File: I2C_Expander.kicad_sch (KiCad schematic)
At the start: 8 parts, among them U501 PCA9554APW

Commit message: Update pcb database to version 6
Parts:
- C501: symbol Custom:C_US_0805_0.1UF_X7R_10%_50V_HS -> custom:C_US_0805_0.1UF_X7R_10%_50V_HS
- R501, R502: symbol Custom:R_US_0805_1%_HS -> custom:R_US_0805_1%_HS; PartNumber 800235-103 -> 800235-XXX
- R503, R504, R505, R506: symbol Custom:R_US_0805_1%_HS -> custom:R_US_0805_1%_HS; PartNumber 800235-102 -> 800235-XXX
- U501: symbol Custom:PCA9554APW -> custom:PCA9554APW
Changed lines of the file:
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@@
     (effects (font (size 1.27 1.27)) (justify left))
   )
-  (symbol (lib_id "Custom:PCA9554APW") (at 163.83 66.04 0)
+  (symbol (lib_id "custom:PCA9554APW") (at 163.83 66.04 0) (unit 1)
     (in_bom yes) (on_board yes)
     (property "Reference" "U501" (id 0) (at 163.83 36.449 0))
@@
     (pin "9")
   )
-  (symbol (lib_id "Custom:GND_US") (at 179.07 91.44 0)
+  (symbol (lib_id "custom:GND_US") (at 179.07 91.44 0) (unit 1)
     (in_bom yes) (on_board yes)
     (property "Reference" "#PWR0503" (id 0) (at 178.562 94.742 0)
@@
     (pin "1")
   )
-  (symbol (lib_id "Custom:C_US_0805_0.1UF_X7R_10%_50V_HS") (at 190.5 39.37 90)
+  (symbol (lib_id "custom:C_US_0805_0.1UF_X7R_10%_50V_HS") (at 190.5 39.37 90) (unit 1)
     (in_bom yes) (on_board yes)
     (property "Reference" "C501" (id 0) (at 190.5 32.5882 90))
@@
     (pin "2")
   )
-  (symbol (lib_id "Custom:P3V3") (at 179.07 26.67 0)
+  (symbol (lib_id "custom:P3V3") (at 179.07 26.67 0) (unit 1)
     (in_bom yes) (on_board yes)
     (property "Reference" "#PWR0501" (id 0) (at 181.61 25.4 0)
@@
     (pin "1")
   )
-  (symbol (lib_id "Custom:GND_US") (at 198.12 41.91 0)
+  (symbol (lib_id "custom:GND_US") (at 198.12 41.91 0) (unit 1)
     (in_bom yes) (on_board yes)
     (property "Reference" "#PWR0502" (id 0) (at 197.612 45.212 0)
@@
     (pin "1")
   )
-  (symbol (lib_id "Custom:R_US_0805_1%_HS") (at 200.66 97.79 0)
+  (symbol (lib_id "custom:R_US_0805_1%_HS") (at 200.66 97.79 0) (unit 1)
     (in_bom yes) (on_board yes)
     (property "Reference" "R503" (id 0) (at 202.184 96.6216 0)
@@
       (effects (font (size 1.524 1.524)))
     )
-    (property "PartNumber" "800235-102" (id 4) (at 205.232 95.25 90)
-      (effects (font (size 1.524 1.524)) hide)
-    )
-    (pin "1")
-    (pin "2")
-  )
-  (symbol (lib_id "Custom:R_US_0805_1%_HS") (at 207.01 97.79 0)
+    (property "PartNumber" "800235-XXX" (id 4) (at 205.232 95.25 90)
+      (effects (font (size 1.524 1.524)) hide)
+    )
+    (pin "1")
+    (pin "2")
+  )
+  (symbol (lib_id "custom:R_US_0805_1%_HS") (at 207.01 97.79 0) (unit 1)
     (in_bom yes) (on_board yes)
     (property "Reference" "R504" (id 0) (at 208.534 96.6216 0)
@@
       (effects (font (size 1.524 1.524)))
     )
-    (property "PartNumber" "800235-102" (id 4) (at 211.582 95.25 90)
-      (effects (font (size 1.524 1.524)) hide)
-    )
-    (pin "1")
-    (pin "2")
-  )
-  (symbol (lib_id "Custom:R_US_0805_1%_HS") (at 213.36 97.79 0)
+    (property "PartNumber" "800235-XXX" (id 4) (at 211.582 95.25 90)
+      (effects (font (size 1.524 1.524)) hide)
+    )
+    (pin "1")
+    (pin "2")
+  )
+  (symbol (lib_id "custom:R_US_0805_1%_HS") (at 213.36 97.79 0) (unit 1)
     (in_bom yes) (on_board yes)
     (property "Reference" "R505" (id 0) (at 214.884 96.6216 0)
@@
       (effects (font (size 1.524 1.524)))
     )
-    (property "PartNumber" "800235-102" (id 4) (at 217.932 95.25 90)
-      (effects (font (size 1.524 1.524)) hide)
-    )
-    (pin "1")
-    (pin "2")
-  )
-  (symbol (lib_id "Custom:R_US_0805_1%_HS") (at 226.06 97.79 0)
+    (property "PartNumber" "800235-XXX" (id 4) (at 217.932 95.25 90)
+      (effects (font (size 1.524 1.524)) hide)
+    )
+    (pin "1")
+    (pin "2")
+  )
+  (symbol (lib_id "custom:R_US_0805_1%_HS") (at 226.06 97.79 0) (unit 1)
     (in_bom yes) (on_board yes)
     (property "Reference" "R506" (id 0) (at 227.584 96.6216 0)
@@
       (effects (font (size 1.524 1.524)))
     )
-    (property "PartNumber" "800235-102" (id 4) (at 230.632 95.25 90)
-      (effects (font (size 1.524 1.524)) hide)
-    )
-    (pin "1")
-    (pin "2")
-  )
-  (symbol (lib_id "Custom:GND_US") (at 200.66 105.41 0)
+    (property "PartNumber" "800235-XXX" (id 4) (at 230.632 95.25 90)
+      (effects (font (size 1.524 1.524)) hide)
+    )
+    (pin "1")
+    (pin "2")
+  )
+  (symbol (lib_id "custom:GND_US") (at 200.66 105.41 0) (unit 1)
     (in_bom yes) (on_board yes)
     (property "Reference" "#PWR0505" (id 0) (at 200.152 108.712 0)
@@
     (pin "1")
   )
-  (symbol (lib_id "Custom:GND_US") (at 207.01 105.41 0)
+  (symbol (lib_id "custom:GND_US") (at 207.01 105.41 0) (unit 1)
     (in_bom yes) (on_board yes)
     (property "Reference" "#PWR0506" (id 0) (at 206.502 108.712 0)
@@
     (pin "1")
   )
-  (symbol (lib_id "Custom:GND_US") (at 213.36 105.41 0)
+  (symbol (lib_id "custom:GND_US") (at 213.36 105.41 0) (unit 1)
     (in_bom yes) (on_board yes)
     (property "Reference" "#PWR0507" (id 0) (at 212.852 108.712 0)
@@
     (pin "1")
   )
-  (symbol (lib_id "Custom:GND_US") (at 226.06 105.41 0)
+  (symbol (lib_id "custom:GND_US") (at 226.06 105.41 0) (unit 1)
     (in_bom yes) (on_board yes)
     (property "Reference" "#PWR0508" (id 0) (at 225.552 108.712 0)
@@
     (pin "1")
   )
-  (symbol (lib_id "Custom:R_US_0805_1%_HS") (at 128.27 34.29 0)
+  (symbol (lib_id "custom:R_US_0805_1%_HS") (at 128.27 34.29 0) (unit 1)
     (in_bom yes) (on_board yes)
     (property "Reference" "R502" (id 0) (at 129.794 33.1216 0)
@@
       (effects (font (size 1.524 1.524)))
     )
-    (property "PartNumber" "800235-103" (id 4) (at 132.842 31.75 90)
-      (effects (font (size 1.524 1.524)) hide)
-    )
-    (pin "1")
-    (pin "2")
-  )
-  (symbol (lib_id "Custom:R_US_0805_1%_HS") (at 115.57 34.29 0)
+    (property "PartNumber" "800235-XXX" (id 4) (at 132.842 31.75 90)
+      (effects (font (size 1.524 1.524)) hide)
+    )
+    (pin "1")
+    (pin "2")
+  )
+  (symbol (lib_id "custom:R_US_0805_1%_HS") (at 115.57 34.29 0) (unit 1)
     (in_bom yes) (on_board yes)
     (property "Reference" "R501" (id 0) (at 117.094 33.1216 0)
@@
       (effects (font (size 1.524 1.524)))
     )
-    (property "PartNumber" "800235-103" (id 4) (at 120.142 31.75 90)
-      (effects (font (size 1.524 1.524)) hide)
-    )
-    (pin "1")
-    (pin "2")
-  )
-  (symbol (lib_id "Custom:GND_US") (at 147.32 104.14 0)
+    (property "PartNumber" "800235-XXX" (id 4) (at 120.142 31.75 90)
+      (effects (font (size 1.524 1.524)) hide)
+    )
+    (pin "1")
+    (pin "2")
+  )
+  (symbol (lib_id "custom:GND_US") (at 147.32 104.14 0) (unit 1)
     (in_bom yes) (on_board yes)
     (property "Reference" "#PWR0504" (id 0) (at 146.812 107.442 0)

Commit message: Fix BOM part number errors and out of sync footprints which happened during conversion from Kicad 5 to 6
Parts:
- R501, R502: PartNumber 800235-XXX -> 800235-103
- R503, R504, R505, R506: PartNumber 800235-XXX -> 800235-102
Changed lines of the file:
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@@
       (effects (font (size 1.524 1.524)))
     )
-    (property "PartNumber" "800235-XXX" (id 4) (at 205.232 95.25 90)
+    (property "PartNumber" "800235-102" (id 4) (at 205.232 95.25 90)
       (effects (font (size 1.524 1.524)) hide)
     )
@@
       (effects (font (size 1.524 1.524)))
     )
-    (property "PartNumber" "800235-XXX" (id 4) (at 211.582 95.25 90)
+    (property "PartNumber" "800235-102" (id 4) (at 211.582 95.25 90)
       (effects (font (size 1.524 1.524)) hide)
     )
@@
       (effects (font (size 1.524 1.524)))
     )
-    (property "PartNumber" "800235-XXX" (id 4) (at 217.932 95.25 90)
+    (property "PartNumber" "800235-102" (id 4) (at 217.932 95.25 90)
       (effects (font (size 1.524 1.524)) hide)
     )
@@
       (effects (font (size 1.524 1.524)))
     )
-    (property "PartNumber" "800235-XXX" (id 4) (at 230.632 95.25 90)
+    (property "PartNumber" "800235-102" (id 4) (at 230.632 95.25 90)
       (effects (font (size 1.524 1.524)) hide)
     )
@@
       (effects (font (size 1.524 1.524)))
     )
-    (property "PartNumber" "800235-XXX" (id 4) (at 132.842 31.75 90)
+    (property "PartNumber" "800235-103" (id 4) (at 132.842 31.75 90)
       (effects (font (size 1.524 1.524)) hide)
     )
@@
       (effects (font (size 1.524 1.524)))
     )
-    (property "PartNumber" "800235-XXX" (id 4) (at 120.142 31.75 90)
+    (property "PartNumber" "800235-103" (id 4) (at 120.142 31.75 90)
       (effects (font (size 1.524 1.524)) hide)
     )

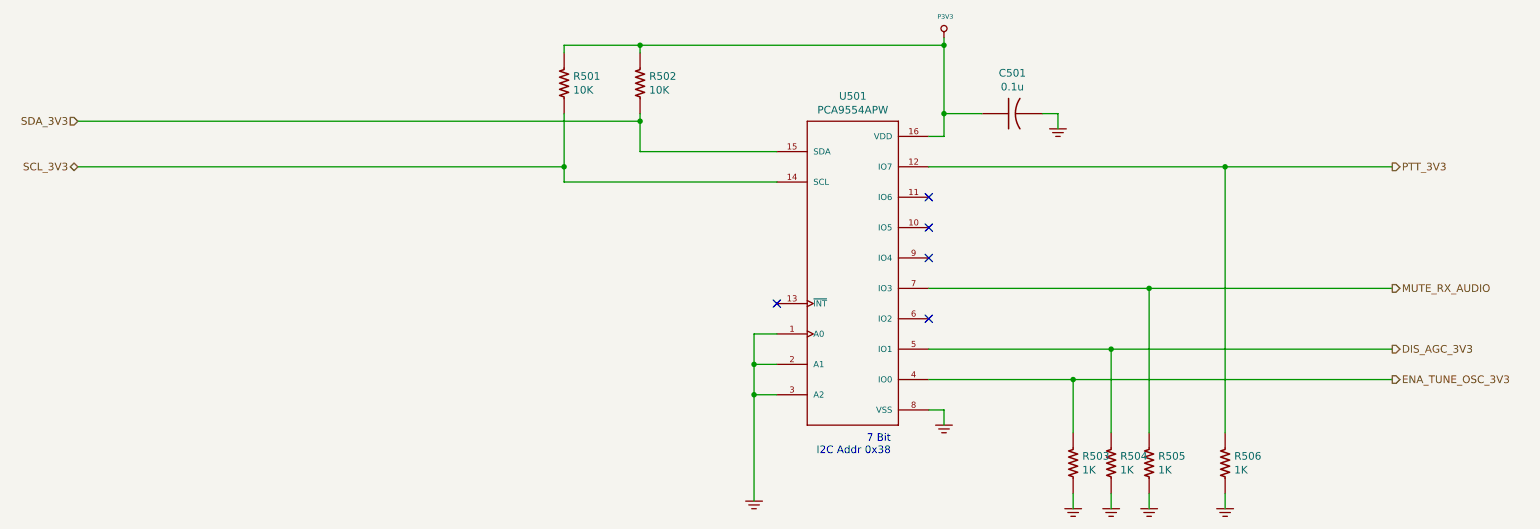
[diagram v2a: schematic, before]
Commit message: trx_mobo_concept_2_B. Change design to use a dedicated 8V supply for the 2SC3357 parts. Add S-Meter connector. Change mic connector to 3 pins and add 8V sopower supply to pin 3.
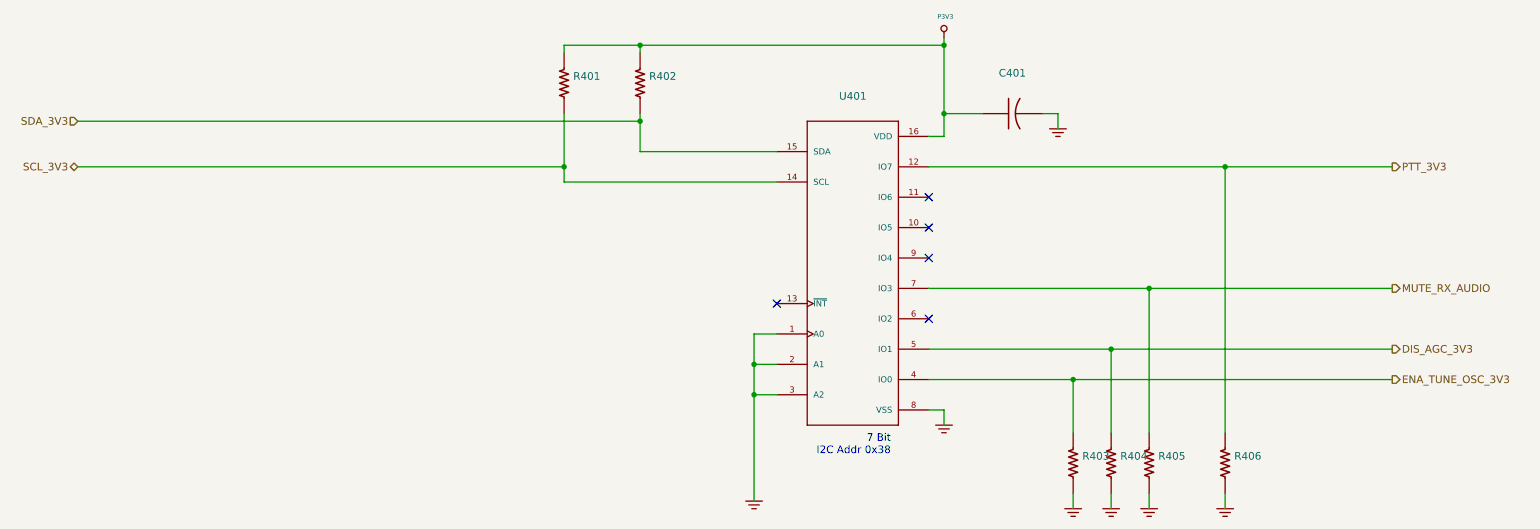
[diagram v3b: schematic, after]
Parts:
- C401: renamed from C501; value 0.1u -> (none); footprint Capacitor_SMD:C_0805_2012Metric_Pad1.15x1.40mm_HandSolder -> (none)
- R401: renamed from R501; value 10K -> (none); footprint Resistor_SMD:R_0805_2012Metric_Pad1.15x1.40mm_HandSolder -> (none)
- R402: renamed from R502; value 10K -> (none); footprint Resistor_SMD:R_0805_2012Metric_Pad1.15x1.40mm_HandSolder -> (none)
- R403: renamed from R503; value 1K -> (none); footprint Resistor_SMD:R_0805_2012Metric_Pad1.15x1.40mm_HandSolder -> (none)
- R404: renamed from R504; value 1K -> (none); footprint Resistor_SMD:R_0805_2012Metric_Pad1.15x1.40mm_HandSolder -> (none)
- R405: renamed from R505; value 1K -> (none); footprint Resistor_SMD:R_0805_2012Metric_Pad1.15x1.40mm_HandSolder -> (none)
- R406: renamed from R506; value 1K -> (none); footprint Resistor_SMD:R_0805_2012Metric_Pad1.15x1.40mm_HandSolder -> (none)
- U401: renamed from U501; value PCA9554APW -> (none); footprint Package_SO:TSSOP-16_4.4x5mm_P0.65mm -> (none)
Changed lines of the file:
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@@
   (paper "A4")
   (title_block
-    (rev "X1")
+    (rev "B")
   )
   (junction (at 128.27 27.94) (diameter 0) (color 0 0 0 0)
@@
   (symbol (lib_id "custom:PCA9554APW") (at 163.83 66.04 0) (unit 1)
     (in_bom yes) (on_board yes)
-    (property "Reference" "U501" (id 0) (at 163.83 36.449 0))
-    (property "Value" "PCA9554APW" (id 1) (at 163.83 38.7604 0))
-    (property "Footprint" "Package_SO:TSSOP-16_4.4x5mm_P0.65mm" (id 2) (at 162.56 93.98 0)
+    (property "Reference" "U401" (id 0) (at 163.83 36.449 0))
+    (property "Value" "" (id 1) (at 163.83 38.7604 0))
+    (property "Footprint" "" (id 2) (at 162.56 93.98 0)
       (effects (font (size 1.27 1.27)) hide)
     )
@@
   (symbol (lib_id "custom:GND_US") (at 179.07 91.44 0) (unit 1)
     (in_bom yes) (on_board yes)
-    (property "Reference" "#PWR0503" (id 0) (at 178.562 94.742 0)
+    (property "Reference" "#PWR0403" (id 0) (at 178.562 94.742 0)
       (effects (font (size 0.762 0.762)) hide)
     )
@@
   (symbol (lib_id "custom:C_US_0805_0.1UF_X7R_10%_50V_HS") (at 190.5 39.37 90) (unit 1)
     (in_bom yes) (on_board yes)
-    (property "Reference" "C501" (id 0) (at 190.5 32.5882 90))
-    (property "Value" "0.1u" (id 1) (at 190.5 34.8996 90))
-    (property "Footprint" "Capacitor_SMD:C_0805_2012Metric_Pad1.15x1.40mm_HandSolder" (id 2) (at 179.07 36.83 0)
+    (property "Reference" "C401" (id 0) (at 190.5 32.5882 90))
+    (property "Value" "" (id 1) (at 190.5 34.8996 90))
+    (property "Footprint" "" (id 2) (at 179.07 36.83 0)
       (effects (font (size 1.524 1.524)) hide)
     )
@@
   (symbol (lib_id "custom:P3V3") (at 179.07 26.67 0) (unit 1)
     (in_bom yes) (on_board yes)
-    (property "Reference" "#PWR0501" (id 0) (at 181.61 25.4 0)
+    (property "Reference" "#PWR0401" (id 0) (at 181.61 25.4 0)
       (effects (font (size 0.762 0.762)) hide)
     )
@@
   (symbol (lib_id "custom:GND_US") (at 198.12 41.91 0) (unit 1)
     (in_bom yes) (on_board yes)
-    (property "Reference" "#PWR0502" (id 0) (at 197.612 45.212 0)
+    (property "Reference" "#PWR0402" (id 0) (at 197.612 45.212 0)
       (effects (font (size 0.762 0.762)) hide)
     )
@@
   (symbol (lib_id "custom:R_US_0805_1%_HS") (at 200.66 97.79 0) (unit 1)
     (in_bom yes) (on_board yes)
-    (property "Reference" "R503" (id 0) (at 202.184 96.6216 0)
-      (effects (font (size 1.27 1.27)) (justify left))
-    )
-    (property "Value" "1K" (id 1) (at 202.184 98.933 0)
-      (effects (font (size 1.27 1.27)) (justify left))
-    )
-    (property "Footprint" "Resistor_SMD:R_0805_2012Metric_Pad1.15x1.40mm_HandSolder" (id 2) (at 200.66 97.79 0)
+    (property "Reference" "R403" (id 0) (at 202.184 96.6216 0)
+      (effects (font (size 1.27 1.27)) (justify left))
+    )
+    (property "Value" "" (id 1) (at 202.184 98.933 0)
+      (effects (font (size 1.27 1.27)) (justify left))
+    )
+    (property "Footprint" "" (id 2) (at 200.66 97.79 0)
       (effects (font (size 1.524 1.524)) hide)
     )
@@
   (symbol (lib_id "custom:R_US_0805_1%_HS") (at 207.01 97.79 0) (unit 1)
     (in_bom yes) (on_board yes)
-    (property "Reference" "R504" (id 0) (at 208.534 96.6216 0)
-      (effects (font (size 1.27 1.27)) (justify left))
-    )
-    (property "Value" "1K" (id 1) (at 208.534 98.933 0)
-      (effects (font (size 1.27 1.27)) (justify left))
-    )
-    (property "Footprint" "Resistor_SMD:R_0805_2012Metric_Pad1.15x1.40mm_HandSolder" (id 2) (at 207.01 97.79 0)
+    (property "Reference" "R404" (id 0) (at 208.534 96.6216 0)
+      (effects (font (size 1.27 1.27)) (justify left))
+    )
+    (property "Value" "" (id 1) (at 208.534 98.933 0)
+      (effects (font (size 1.27 1.27)) (justify left))
+    )
+    (property "Footprint" "" (id 2) (at 207.01 97.79 0)
       (effects (font (size 1.524 1.524)) hide)
     )
@@
   (symbol (lib_id "custom:R_US_0805_1%_HS") (at 213.36 97.79 0) (unit 1)
     (in_bom yes) (on_board yes)
-    (property "Reference" "R505" (id 0) (at 214.884 96.6216 0)
-      (effects (font (size 1.27 1.27)) (justify left))
-    )
-    (property "Value" "1K" (id 1) (at 214.884 98.933 0)
-      (effects (font (size 1.27 1.27)) (justify left))
-    )
-    (property "Footprint" "Resistor_SMD:R_0805_2012Metric_Pad1.15x1.40mm_HandSolder" (id 2) (at 213.36 97.79 0)
+    (property "Reference" "R405" (id 0) (at 214.884 96.6216 0)
+      (effects (font (size 1.27 1.27)) (justify left))
+    )
+    (property "Value" "" (id 1) (at 214.884 98.933 0)
+      (effects (font (size 1.27 1.27)) (justify left))
+    )
+    (property "Footprint" "" (id 2) (at 213.36 97.79 0)
       (effects (font (size 1.524 1.524)) hide)
     )
@@
   (symbol (lib_id "custom:R_US_0805_1%_HS") (at 226.06 97.79 0) (unit 1)
     (in_bom yes) (on_board yes)
-    (property "Reference" "R506" (id 0) (at 227.584 96.6216 0)
-      (effects (font (size 1.27 1.27)) (justify left))
-    )
-    (property "Value" "1K" (id 1) (at 227.584 98.933 0)
-      (effects (font (size 1.27 1.27)) (justify left))
-    )
-    (property "Footprint" "Resistor_SMD:R_0805_2012Metric_Pad1.15x1.40mm_HandSolder" (id 2) (at 226.06 97.79 0)
+    (property "Reference" "R406" (id 0) (at 227.584 96.6216 0)
+      (effects (font (size 1.27 1.27)) (justify left))
+    )
+    (property "Value" "" (id 1) (at 227.584 98.933 0)
+      (effects (font (size 1.27 1.27)) (justify left))
+    )
+    (property "Footprint" "" (id 2) (at 226.06 97.79 0)
       (effects (font (size 1.524 1.524)) hide)
     )
@@
   (symbol (lib_id "custom:GND_US") (at 200.66 105.41 0) (unit 1)
     (in_bom yes) (on_board yes)
-    (property "Reference" "#PWR0505" (id 0) (at 200.152 108.712 0)
+    (property "Reference" "#PWR0405" (id 0) (at 200.152 108.712 0)
       (effects (font (size 0.762 0.762)) hide)
     )
@@
   (symbol (lib_id "custom:GND_US") (at 207.01 105.41 0) (unit 1)
     (in_bom yes) (on_board yes)
-    (property "Reference" "#PWR0506" (id 0) (at 206.502 108.712 0)
+    (property "Reference" "#PWR0406" (id 0) (at 206.502 108.712 0)
       (effects (font (size 0.762 0.762)) hide)
     )
@@
   (symbol (lib_id "custom:GND_US") (at 213.36 105.41 0) (unit 1)
     (in_bom yes) (on_board yes)
-    (property "Reference" "#PWR0507" (id 0) (at 212.852 108.712 0)
+    (property "Reference" "#PWR0407" (id 0) (at 212.852 108.712 0)
       (effects (font (size 0.762 0.762)) hide)
     )
@@
   (symbol (lib_id "custom:GND_US") (at 226.06 105.41 0) (unit 1)
     (in_bom yes) (on_board yes)
-    (property "Reference" "#PWR0508" (id 0) (at 225.552 108.712 0)
+    (property "Reference" "#PWR0408" (id 0) (at 225.552 108.712 0)
       (effects (font (size 0.762 0.762)) hide)
     )
@@
   (symbol (lib_id "custom:R_US_0805_1%_HS") (at 128.27 34.29 0) (unit 1)
     (in_bom yes) (on_board yes)
-    (property "Reference" "R502" (id 0) (at 129.794 33.1216 0)
-      (effects (font (size 1.27 1.27)) (justify left))
-    )
-    (property "Value" "10K" (id 1) (at 129.794 35.433 0)
-      (effects (font (size 1.27 1.27)) (justify left))
-    )
-    (property "Footprint" "Resistor_SMD:R_0805_2012Metric_Pad1.15x1.40mm_HandSolder" (id 2) (at 128.27 34.29 0)
+    (property "Reference" "R402" (id 0) (at 129.794 33.1216 0)
+      (effects (font (size 1.27 1.27)) (justify left))
+    )
+    (property "Value" "" (id 1) (at 129.794 35.433 0)
+      (effects (font (size 1.27 1.27)) (justify left))
+    )
+    (property "Footprint" "" (id 2) (at 128.27 34.29 0)
       (effects (font (size 1.524 1.524)) hide)
     )
@@
   (symbol (lib_id "custom:R_US_0805_1%_HS") (at 115.57 34.29 0) (unit 1)
     (in_bom yes) (on_board yes)
-    (property "Reference" "R501" (id 0) (at 117.094 33.1216 0)
-      (effects (font (size 1.27 1.27)) (justify left))
-    )
-    (property "Value" "10K" (id 1) (at 117.094 35.433 0)
-      (effects (font (size 1.27 1.27)) (justify left))
-    )
-    (property "Footprint" "Resistor_SMD:R_0805_2012Metric_Pad1.15x1.40mm_HandSolder" (id 2) (at 115.57 34.29 0)
+    (property "Reference" "R401" (id 0) (at 117.094 33.1216 0)
+      (effects (font (size 1.27 1.27)) (justify left))
+    )
+    (property "Value" "" (id 1) (at 117.094 35.433 0)
+      (effects (font (size 1.27 1.27)) (justify left))
+    )
+    (property "Footprint" "" (id 2) (at 115.57 34.29 0)
       (effects (font (size 1.524 1.524)) hide)
     )
@@
   (symbol (lib_id "custom:GND_US") (at 147.32 104.14 0) (unit 1)
     (in_bom yes) (on_board yes)
-    (property "Reference" "#PWR0504" (id 0) (at 146.812 107.442 0)
-      (effects (font (size 0.762 0.762)) hide)
-    )
+    (property "Reference" "#PWR0404" (id 0) (at 146.812 107.442 0)
+      (effects (font (size 0.762 0.762)) hide)
+    )
